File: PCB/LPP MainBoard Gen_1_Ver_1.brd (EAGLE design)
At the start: 50 x 108 mm, 46 parts, among them IC1 FE1.1S, J1 USB Type A, U1 MAX15070, U3 IFX007T, U4 MAX15070, U5 IFX007T, U7 Pill STM32G431, U8 Blue Pill STM32F103

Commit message: modified:   PCB/LPP MainBoard Gen_1_Ver_1.brd 	modified:   PCB/LPP MainBoard Gen_1_Ver_1.dch 	modified:   PCB/LPP MainBoard Gen_1_Ver_1.sch 	modified:   PCB/LPP_MainBoard_Gen_1_Ver_1.dip 	deleted:    PCB/LPP_MainBoard_Gen_1_Ver_1/Through.drl 	new file:   PCB/LPP_MainBoard_Gen_1_Ver_1/komtur.crv3d 	new file:   PCB/LPP_MainBoard_Gen_1_Ver_1/komtur.dxf 	new file:   PCB/LPP_MainBoard_Gen_1_Ver_1/kontur.txt
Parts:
- added R13: R_0805_1206, common:R_0805_1206_R13
- added R14: R_0805_1206, common:R_0805_1206_R14
- LAZERKP: device common:PLS_3_LAZERKP -> common:PLS_3
- moved C8 1.20 mm to (3.70, 87.3)
- moved ENCKP 0.80 mm to (3.70, 80.4)
- moved LAZERKP 0.61 mm to (7.50, 97.8)
- moved XP2 0.40 mm to (9.80, 92.0)
- moved XP3 0.40 mm to (9.80, 94.5)
- moved C11 0.30 mm to (16.5, 94.1)
- moved R4 0.30 mm to (5.30, 93.3)
- moved R2 0.22 mm to (11.8, 85.4)
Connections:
- net Сеть_10: now also R13.2@, R13.2@_1
- net Сеть_6: now also R14.2@, R14.2@_1
- net Сеть_7: now also R13.1@, R13.1@_1, R14.1@, R14.1@_1
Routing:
- net Сеть_10: track 128.7 -> 145.6 mm, vias 3 -> 4
- net Сеть_6: track 95.3 -> 111.5 mm, vias 3 -> 4
- net Сеть_0: track 666.6 -> 679.1 mm
- net Сеть_7: track 237.7 -> 241.9 mm
- net Сеть_16: track 141.5 -> 145.1 mm
- net Сеть_30: track 124.4 -> 126.2 mm, vias 4 -> 3
- net Сеть_49: track 124.0 -> 125.5 mm
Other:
- board text added: "R13"
- board text added: "R14"

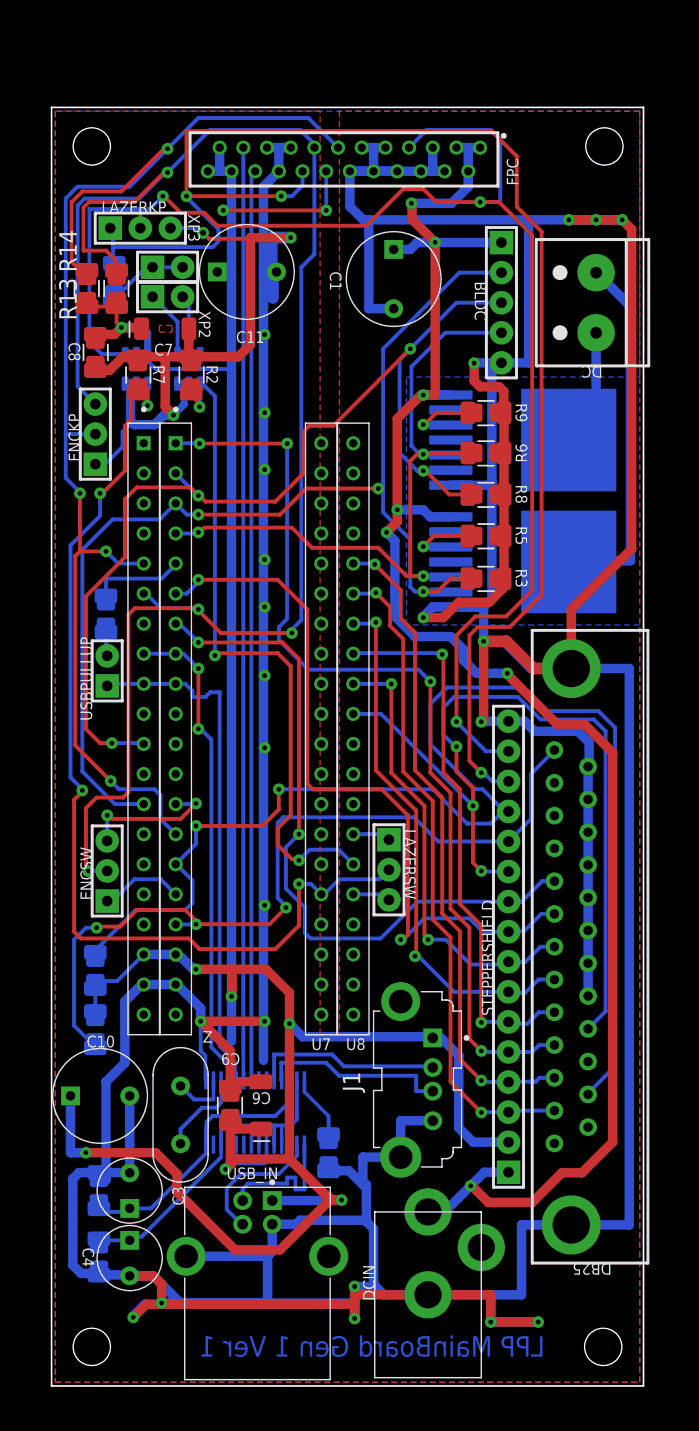
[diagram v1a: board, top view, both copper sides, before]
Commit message: modified:   PCB/LPP MainBoard Gen_1_Ver_1.brd 	modified:   PCB/LPP MainBoard Gen_1_Ver_1.dch 	modified:   PCB/LPP MainBoard Gen_1_Ver_1.sch 	modified:   PCB/LPP_MainBoard_Gen_1_Ver_1.dip 	new file:   PCB/LPP_MainBoard_Gen_1_Ver_1/Through.drl 	new file:   PCB/LPP_MainBoard_Gen_1_Ver_1/Through2.drl 	new file:   PCB/LPP_MainBoard_Gen_1_Ver_1/Through3.drl
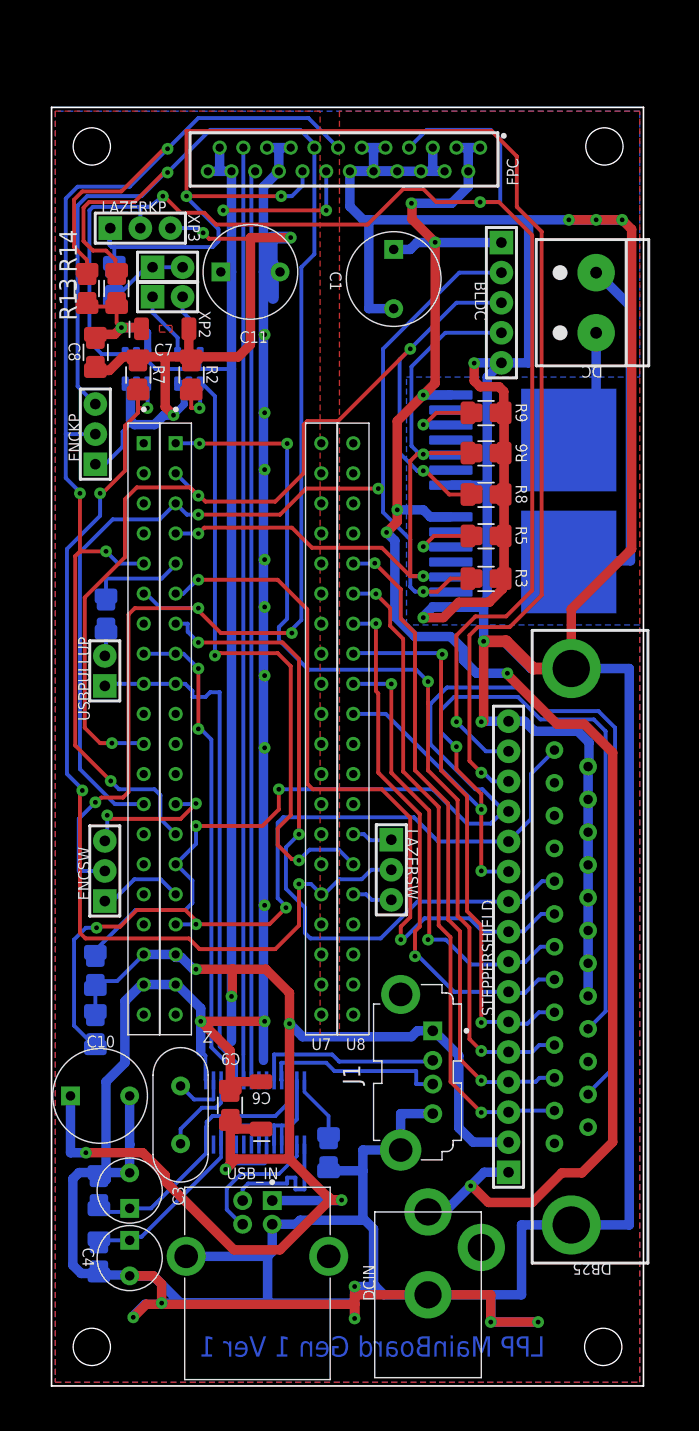
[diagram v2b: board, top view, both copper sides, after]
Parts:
- moved J1 0.60 mm to (30.9, 26.5)
- moved C11 0.30 mm to (16.8, 94.1)
- moved ENCSW 0.20 mm to (4.50, 43.5)
- moved USBPULLUP 0.20 mm to (4.50, 60.4)
- moved LAZERSW 0.20 mm to (28.7, 43.6)
- turned R13 to 810.002 degrees
- turned R14 to 450.001 degrees
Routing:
- net Сеть_0: track 679.1 -> 681.4 mm
- net Сеть_26: track 71.9 -> 72.8 mm
- net Сеть_16: track 145.1 -> 144.4 mm
- net Сеть_38: track 58.0 -> 58.6 mm
- net Сеть_6: track 111.5 -> 111.0 mm

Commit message: modified:   PCB/LPP MainBoard Gen_1_Ver_1.brd 	modified:   PCB/LPP MainBoard Gen_1_Ver_1.sch
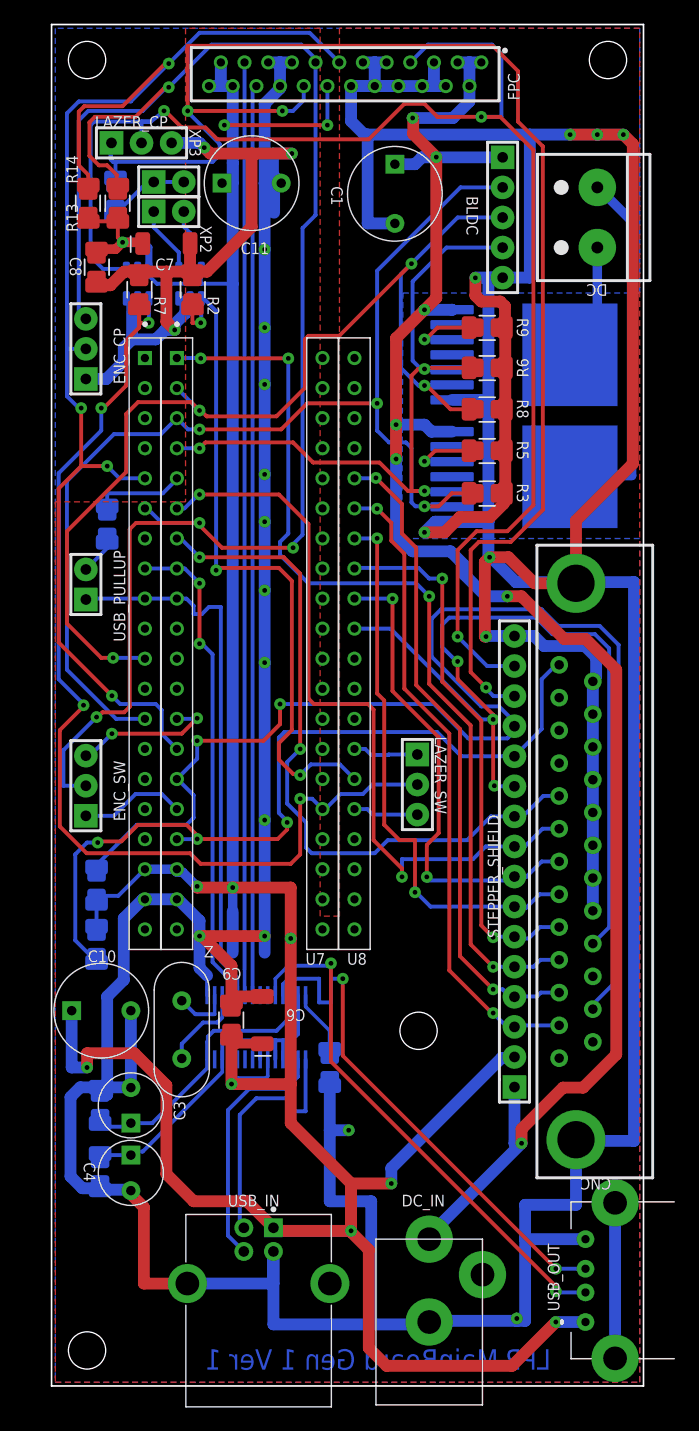
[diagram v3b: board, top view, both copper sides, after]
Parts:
- removed DB25: DB25M, common:DB25M
- removed DCIN: DC IN, common:J-1
- removed ENCKP: ENCKP, common:PLS_3
- removed ENCSW: ENC SW, common:PLS_3
- removed J1: USB Type A, common:USB-1_Type_A
- removed LAZERKP: LAZER, common:PLS_3
- removed LAZERSW: LAZER SW, common:PLS_3
- removed STEPPERSHIELD: STEPPER SHIELD, common:PLS_16
- removed USBPULLUP: USB PULLUP, common:PLS_2
- added CNC: CNC, common:DB25M
- added DC_IN: J-1, common:J-1
- added ENC_CP: ENC CP, common:PLS_3
- added ENC_SW: ENC SW, common:PLS_3
- added LAZER_CP: LAZER_CP, common:PLS_3_LAZER_CP
- added LAZER_SW: LAZER SW, common:PLS_3_LAZER_CP
- added STEPPER_SHIELD: STEPPER SHIELD, common:PLS_16
- added USB_OUT: USB OUT, common:USB_Type_A_horizontal
- added USB_PULLUP: USB PULLUP, common:PLS_2
- R12: device common:R_0805_1206_R4 -> common:R_0805_1206_R12
- U8: device common:ST_Pill -> common:ST_Pill_U8
- moved R10 7.60 mm to (4.70, 72.8)
- moved C11 7.50 mm to (16.9, 101.6)
- moved BLDC 7.20 mm to (38.1, 98.7)
- moved C1 7.20 mm to (29.0, 100.7)
- moved C7 7.20 mm to (9.70, 96.5)
- moved C8 7.20 mm to (3.80, 94.5)
- moved DC 7.20 mm to (46.1, 98.7)
- moved FPC 7.20 mm to (24.3, 110.8)
- moved R13 7.20 mm to (5.60, 99.9)
- moved R14 7.20 mm to (3.10, 99.9), turned to 90 degrees
- moved R3 7.20 mm to (36.8, 75.4)
- moved R4 7.20 mm to (5.40, 100.5)
- moved R5 7.20 mm to (36.8, 79.0)
- moved R6 7.20 mm to (36.8, 86.0)
- moved R8 7.20 mm to (36.8, 82.5)
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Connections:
- net Сеть_0: now also CNC.18, CNC.19, CNC.20, CNC.21, CNC.22, CNC.23, CNC.24, CNC.25, CNC.@26, CNC.@26_1, DC_IN.2, ENC_CP.1, LAZER_CP.3, STEPPER_SHIELD.16, USB_OUT.4, USB_OUT.@5, USB_OUT.@5_1; no longer DB25.18, DB25.19, DB25.20, DB25.21, DB25.22, DB25.23, DB25.24, DB25.25, DB25.@26, DB25.@26_1, DCIN.2, ENCKP.1, J1.4, J1.5@, J1.5@_1, LAZERKP.3, STEPPERSHIELD.16
- net Сеть_10: now also ENC_CP.3, ENC_SW.2; no longer ENCKP.3, ENCSW.2
- net Сеть_11: now also USB_OUT.2; no longer J1.2
- net Сеть_13: now also CNC.3, STEPPER_SHIELD.4; no longer DB25.3, STEPPERSHIELD.4
- net Сеть_16: now also DC_IN.1, STEPPER_SHIELD.1; no longer DCIN.1, STEPPERSHIELD.1
- net Сеть_17: now also CNC.13, STEPPER_SHIELD.12; no longer DB25.13, STEPPERSHIELD.12
- net Сеть_19: now also CNC.5, STEPPER_SHIELD.6; no longer DB25.5, STEPPERSHIELD.6
- net Сеть_20: now also CNC.6, STEPPER_SHIELD.7; no longer DB25.6, STEPPERSHIELD.7
- net Сеть_21: now also CNC.7, STEPPER_SHIELD.8; no longer DB25.7, STEPPERSHIELD.8
- net Сеть_22: now also CNC.8, STEPPER_SHIELD.9; no longer DB25.8, STEPPERSHIELD.9
- net Сеть_25: now also CNC.9, STEPPER_SHIELD.10; no longer DB25.9, STEPPERSHIELD.10
- net Сеть_26: now also CNC.17, STEPPER_SHIELD.11; no longer DB25.17, STEPPERSHIELD.11
- net Сеть_27: now also ENC_SW.1; no longer ENCSW.1
- net Сеть_28: now also ENC_SW.3; no longer ENCSW.3
- net Сеть_29: now also CNC.4, STEPPER_SHIELD.5; no longer DB25.4, STEPPERSHIELD.5
- net Сеть_30: now also LAZER_CP.2, STEPPER_SHIELD.15; no longer LAZERKP.2, STEPPERSHIELD.15
- net Сеть_32: now also CNC.15, STEPPER_SHIELD.13; no longer DB25.15, STEPPERSHIELD.13
- net Сеть_36: now also CNC.2, STEPPER_SHIELD.3; no longer DB25.2, STEPPERSHIELD.3
- net Сеть_37: now also LAZER_SW.2; no longer LAZERSW.2
- net Сеть_40: now also USB_PULLUP.1; no longer USBPULLUP.1
- net Сеть_44: now also LAZER_SW.3; no longer LAZERSW.3
- net Сеть_45: now also LAZER_SW.1; no longer LAZERSW.1
- net Сеть_49: now also LAZER_CP.1, STEPPER_SHIELD.14; no longer LAZERKP.1, STEPPERSHIELD.14
- net Сеть_6: now also ENC_CP.2; no longer ENCKP.2
- net Сеть_7: now also STEPPER_SHIELD.2, USB_OUT.1; no longer J1.1, STEPPERSHIELD.2
- net Сеть_8: now also USB_OUT.3; no longer J1.3
- net Сеть_9: now also USB_PULLUP.2; no longer USBPULLUP.2
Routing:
- net Сеть_0: track 681.4 -> 624.0 mm, vias 26 -> 22
- net Сеть_7: track 241.4 -> 285.4 mm, vias 9 -> 11
- net Сеть_8: track 15.7 -> 44.6 mm, vias 0 -> 2
- net Сеть_11: track 15.9 -> 44.9 mm, vias 0 -> 2
- net Сеть_24: track 11.7 -> 21.5 mm
- net Сеть_15: track 11.7 -> 21.1 mm
- net Сеть_16: track 144.4 -> 149.6 mm
- net Сеть_37: track 86.0 -> 91.0 mm
- net Сеть_21: track 38.4 -> 40.9 mm
- net Сеть_45: track 3.44 -> 5.54 mm
- net Сеть_44: track 3.41 -> 5.51 mm
- net Сеть_40: track 44.2 -> 46.0 mm
- net Сеть_20: track 45.3 -> 47.1 mm
- net Сеть_34: track 96.3 -> 98.1 mm
- net Сеть_27: track 7.27 -> 8.97 mm
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- removed copper zone on layer 1, net N$1
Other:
- board size 50 x 108 mm -> 50 x 115 mm
- board text added: "CNC"
- board text added: "DC_IN"
- board text added: "ENC_CP"
- board text added: "ENC_SW"
- board text added: "LAZER_CP"
- board text added: "LAZER_SW"
- board text added: "STEPPER_SHIELD"
- board text added: "USB_OUT"
- board text added: "USB_PULLUP"
- board text removed: "DB25"
- board text removed: "DCIN"
- board text removed: "ENCKP"
- board text removed: "ENCSW"
- board text removed: "J1"
- board text removed: "LAZERKP"
- board text removed: "LAZERSW"
- board text removed: "STEPPERSHIELD"
- board text removed: "USBPULLUP"

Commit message: modified:   PCB/LPP MainBoard Gen_1_Ver_1.brd 	modified:   PCB/LPP MainBoard Gen_1_Ver_1.sch 	modified:   PCB/LPP_MainBoard_Gen_1_Ver_1.dch 	modified:   PCB/LPP_MainBoard_Gen_1_Ver_1.dip
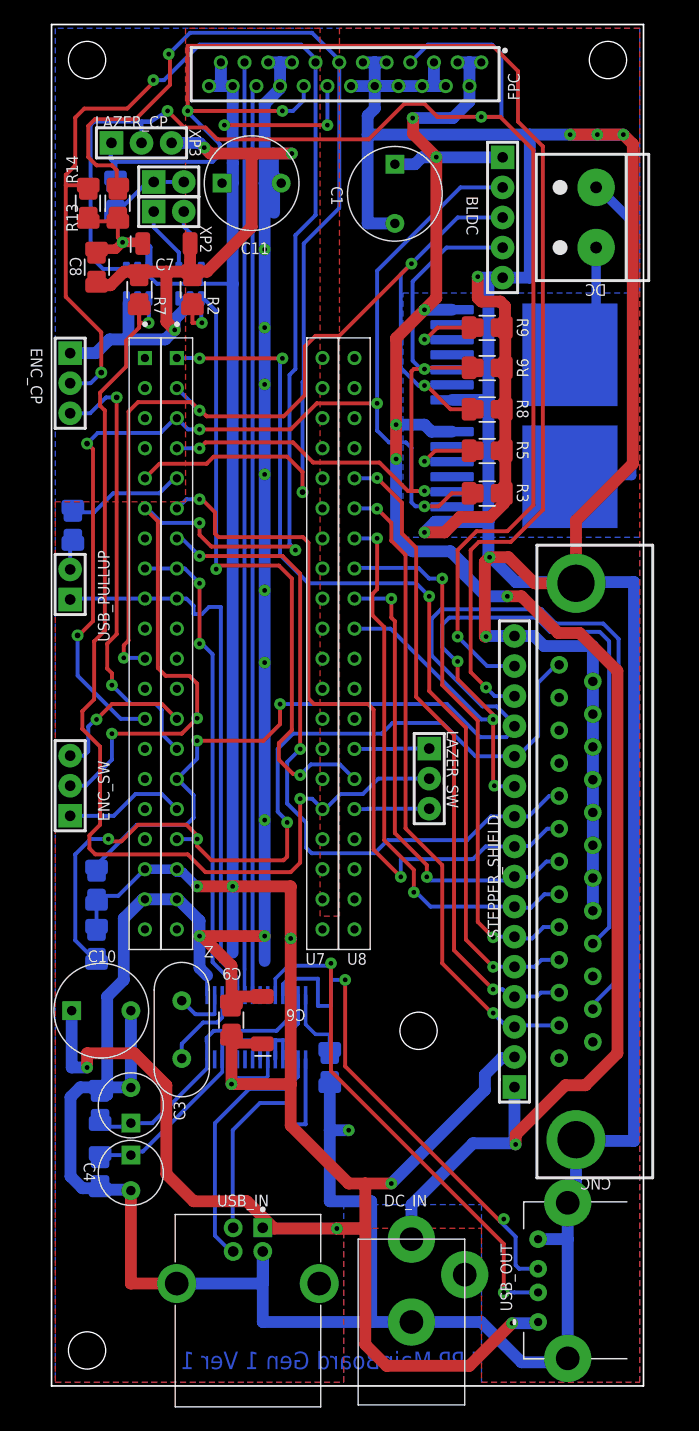
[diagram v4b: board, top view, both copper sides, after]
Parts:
- R1: value R_0805_1206 -> 2.7 Kom
- moved USB_OUT 4.00 mm to (43.6, 8.90)
- moved ENC_CP 3.19 mm to (1.57, 84.7), turned to 270 degrees
- moved R10 2.90 mm to (1.80, 72.7)
- moved DC_IN 1.50 mm to (30.4, 5.40)
- moved ENC_SW 1.33 mm to (1.57, 50.7)
- moved USB_PULLUP 1.33 mm to (1.57, 67.7)
- moved LAZER_SW 1.12 mm to (31.9, 51.3)
- moved USB_IN 0.90 mm to (16.6, 8.70)
- moved DC 0.10 mm to (46.0, 98.7)
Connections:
- new net Сеть_33: ENC_CP.2, ENC_SW.2, FPC.15, R14.2@, R14.2@_1, U7.6
- net Сеть_10: now also FPC.13, U7.5; no longer ENC_CP.3, ENC_SW.2, FPC.15, U7.6
- net Сеть_6: now also ENC_CP.3; no longer ENC_CP.2, FPC.13, R14.2@, R14.2@_1, U7.5
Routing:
- net Сеть_33: track 0.00 -> 144.1 mm, vias 0 -> 6
- net Сеть_6: track 111.2 -> 38.2 mm, vias 4 -> 2
- net Сеть_10: track 144.8 -> 88.7 mm, vias 4 -> 2
- net Сеть_0: track 624.0 -> 610.5 mm, vias 22 -> 20
- net Сеть_7: track 285.4 -> 280.2 mm
- net Сеть_35: track 91.7 -> 86.6 mm
- net Сеть_17: track 70.0 -> 73.7 mm
- net Сеть_4: track 7.53 -> 10.4 mm
- net Сеть_16: track 149.6 -> 151.9 mm
- net Сеть_40: track 46.0 -> 47.4 mm
- net Сеть_27: track 8.97 -> 10.3 mm
- net Сеть_24: track 21.5 -> 22.7 mm
- net Сеть_11: track 44.9 -> 43.7 mm
- net Сеть_21: track 40.9 -> 40.0 mm
- net Сеть_44: track 5.51 -> 6.33 mm
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
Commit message: modified:   LPP_STM32F103Cx/Core/Src/main.c 	modified:   LPP_STM32F103Cx/LPP_STM32F103Cx.ioc 	modified:   LPP_STM32F103Cx/MDK-ARM/JLinkLog.txt 	modified:   LPP_STM32F103Cx/MDK-ARM/LPP_STM32F103Cx.uvguix.user 	modified:   LPP_STM32F103Cx/MDK-ARM/LPP_STM32F103Cx/LPP_STM32F103Cx.axf 	modified:   LPP_STM32F103Cx/MDK-ARM/LPP_STM32F103Cx/LPP_STM32F103Cx.build_log.htm 	modified:   LPP_STM32F103Cx/MDK-ARM/LPP_STM32F103Cx/LPP_STM32F103Cx.hex 	modified:   LPP_STM32F103Cx/MDK-ARM/LPP_STM32F103Cx/LPP_STM32F103Cx.htm 	modified:   LPP_STM32F103Cx/MDK-ARM/LPP_STM32F103Cx/LPP_STM32F103Cx.map 	modified:   LPP_STM32F103Cx/MDK-ARM/LPP_STM32F103Cx/LPP_STM32F103Cx_LPP_STM32F103Cx.dep 	modified:   LPP_STM32F103Cx/MDK-ARM/LPP_STM32F103Cx/main.o 	modified:   LPP_STM32F103Cx/MDK-ARM/counter.txt 	modified:   LPP_STM32F103Cx/My_Libraries/counter.h 	modified:   PCB/LPP MainBoard Gen_1_Ver_1.brd 	modified:   PCB/LPP MainBoard Gen_1_Ver_1.sch 	new file:   "PCB/LPP_MainBoard_Gen_1_Ver_1 \342\200\224 \320\272\320\276\320\277\320\270\321\217.dch" 	new file:   "PCB/LPP_MainBoard_Gen_1_Ver_1 \342\200\224 \320\272\320\276\320\277\320\270\321\217.dip" 	modified:   PCB/LPP_MainBoard_Gen_1_Ver_1.dch 	modified:   PCB/LPP_MainBoard_Gen_1_Ver_1.dip 	deleted:    "PCB/LPP_MainBoard_Gen_1_Ver_1/1 - \320\222\320\265\321\200\321\205\320\275\320\270\320\271.gbr" 	deleted:    "PCB/LPP_MainBoard_Gen_1_Ver_1/2 - \320\235\320\270\320\266\320\275\320\270\320\271.gbr" 	deleted:    PCB/LPP_MainBoard_Gen_1_Ver_1/Bord.lpp 	deleted:    PCB/LPP_MainBoard_Gen_1_Ver_1/Through.txt 	deleted:    PCB/LPP_MainBoard_Gen_1_Ver_1/komtur.crv3d 	deleted:    PCB/LPP_MainBoard_Gen_1_Ver_1/komtur.dxf 	deleted:    PCB/LPP_MainBoard_Gen_1_Ver_1/kontur.txt 	modified:   PCB/README.md
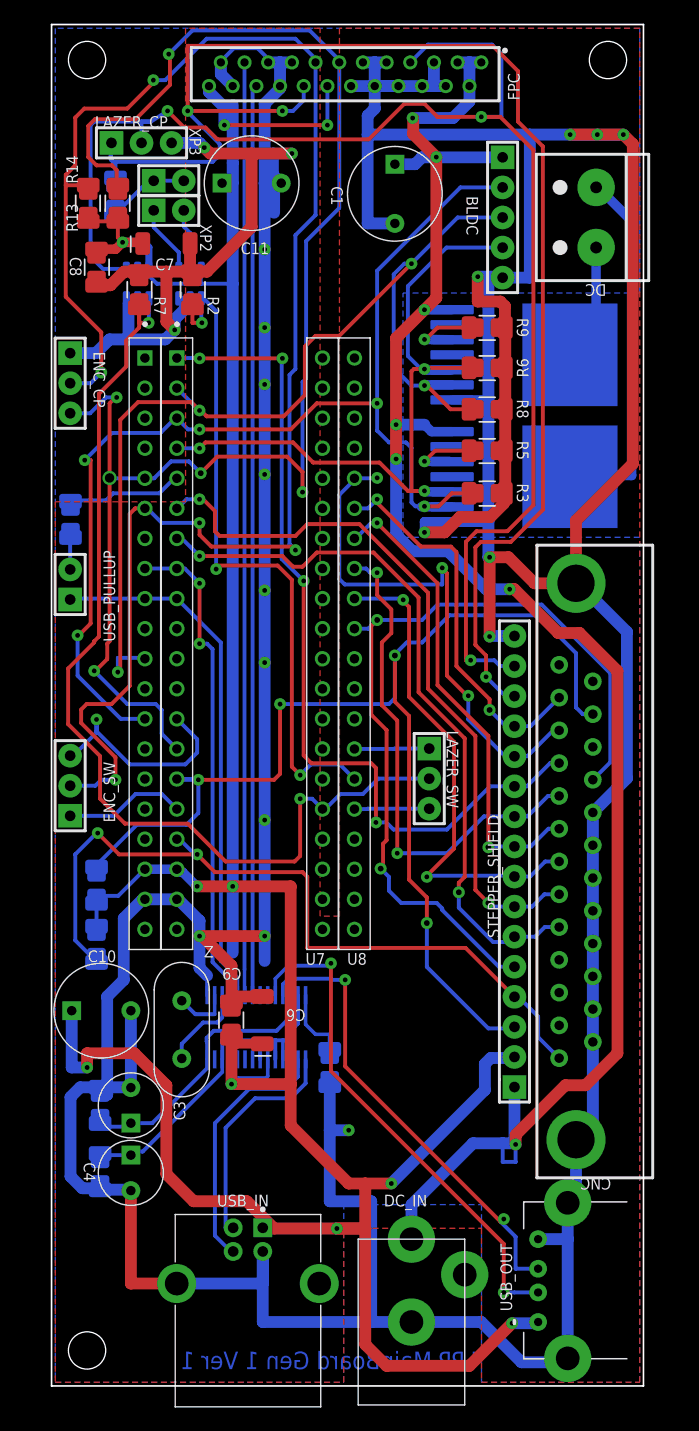
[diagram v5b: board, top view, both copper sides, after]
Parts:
- C3, C4: value CAP_P_3MM -> 10 mf
- CNC: value CNC -> DB25M
- DC_IN: value J-1 -> DC-005-5.5-2.1
- ENC_SW: device common:PLS_3 -> common:PLS_3_ENC_SW
- R10: value R_0805_1206 -> 1.5 k; device common:R_0805_1206_R4 -> common:R_0805_1206_R10
- R5, R9: value R_0805_1206 -> 5.1 k
- U3, U5: value IFX007T -> BTN7933B
- Z: value Q_1 -> 12MHz
- moved R10 0.54 mm to (1.60, 73.2)
- moved XP2 0.10 mm to (9.90, 99.3)
- moved XP3 0.10 mm to (9.90, 101.8)
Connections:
- removed net Сеть_10: FPC.13, R13.2@, R13.2@_1, U7.5
- net Сеть_0: now also FPC.22, FPC.23
- net Сеть_13: now also STEPPER_SHIELD.12; no longer STEPPER_SHIELD.4
- net Сеть_17: now also STEPPER_SHIELD.4; no longer STEPPER_SHIELD.12
- net Сеть_19: now also STEPPER_SHIELD.10; no longer STEPPER_SHIELD.6
- net Сеть_20: now also STEPPER_SHIELD.9; no longer STEPPER_SHIELD.7
- net Сеть_22: now also STEPPER_SHIELD.7; no longer STEPPER_SHIELD.9
- net Сеть_25: now also STEPPER_SHIELD.6; no longer STEPPER_SHIELD.10
- net Сеть_26: now also STEPPER_SHIELD.5; no longer STEPPER_SHIELD.11
- net Сеть_29: now also STEPPER_SHIELD.11; no longer STEPPER_SHIELD.5
- net Сеть_32: now also STEPPER_SHIELD.3; no longer STEPPER_SHIELD.13
- net Сеть_36: now also STEPPER_SHIELD.13; no longer STEPPER_SHIELD.3
- net Сеть_6: now also FPC.13, R13.2@, R13.2@_1, U7.5
- net Сеть_7: no longer FPC.22, FPC.23
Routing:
- net Сеть_6: track 38.2 -> 132.1 mm, vias 2 -> 6
- net Сеть_10: track 88.7 -> 0.00 mm, vias 2 -> 0
- net Сеть_0: track 610.5 -> 574.3 mm
- net Сеть_36: track 54.8 -> 32.9 mm
- net Сеть_13: track 55.2 -> 44.9 mm, vias 2 -> 3
- net Сеть_17: track 73.7 -> 66.1 mm, vias 3 -> 2
- net Сеть_29: track 79.1 -> 72.5 mm
- net Сеть_20: track 46.7 -> 40.4 mm
- net Сеть_28: track 12.6 -> 18.8 mm
- net Сеть_32: track 111.3 -> 105.7 mm, vias 2 -> 4
- net Сеть_35: track 86.6 -> 91.1 mm
- net Сеть_8: track 43.9 -> 39.6 mm
- net Сеть_37: track 90.4 -> 86.3 mm
- net Сеть_16: track 151.9 -> 155.6 mm
- net Сеть_24: track 22.7 -> 19.4 mm
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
